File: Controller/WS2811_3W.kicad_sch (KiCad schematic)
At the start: 19 parts, among them J1 Conn_01x01_Female, J2 Conn_01x01_Female, J3 Conn_01x01_Female, J4 Conn_01x01_Female, J5 Conn_01x01_Female, J6 Conn_01x01_Female, U1 MAX485E, U2 WS2811, U3 MAX485E, U4 AMS1117-5.0

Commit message: pcb stuff
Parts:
- added J10, J11, J12, J7, J8, J9: Conn_01x01_Female, Connector_Wire:SolderWirePad_1x01_SMD_1x2mm, symbol Connector:Conn_01x01_Female
- added R6, R7, R8: 10k, Resistor_SMD:R_0603_1608Metric, symbol Device:R
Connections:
- net +5V: now also R6.1, R7.1, R8.1; no longer U1.8 (VCC)
- net DIM_B: now also R7.2
- net DIM_G: now also R8.2
- net DIM_R: now also R6.2
- net GND: no longer U1.2 (~RE), U1.3 (DE), U1.5 (GND)
- net WS_DIN: no longer U1.1 (RO)
- net at J2.1 (Pin_1), R1.2: no longer U1.6 (A)
- net at J1.1 (Pin_1), R1.1: no longer U1.7 (B)
- new net DCDC_CC/OUT+: J7.1 (Pin_1)
- new net DCDC_CC/OUT-: J8.1 (Pin_1)
- new net DCDC_CC1/OUT+: J9.1 (Pin_1)
- new net DCDC_CC1/OUT-: J10.1 (Pin_1)
- new net DCDC_CC2/OUT+: J11.1 (Pin_1)
- new net DCDC_CC2/OUT-: J12.1 (Pin_1)
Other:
- moved on the sheet: U1

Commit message: finish PCB
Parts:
- J5, J6: footprint Connector_Wire:SolderWirePad_1x01_SMD_1x2mm -> Techbeard:SolderWirePad_1x01_SMD_2x4mm
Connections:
- net +5V: now also U1.8 (VCC)
- net GND: now also U1.2 (~RE), U1.3 (DE), U1.5 (GND)
- net WS_DIN: now also U1.1 (RO)
- net at U1.6 (A): now also J2.1 (Pin_1), R1.2
- net at U1.7 (B): now also J1.1 (Pin_1), R1.1
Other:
- moved on the sheet: U1
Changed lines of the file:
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@@
     (property "Reference" "J5" (id 0) (at 170.3324 62.23 0))
     (property "Value" "Conn_01x01_Female" (id 1) (at 169.0624 67.31 0))
-    (property "Footprint" "Connector_Wire:SolderWirePad_1x01_SMD_1x2mm" (id 2) (at 168.91 64.77 0)
+    (property "Footprint" "Techbeard:SolderWirePad_1x01_SMD_2x4mm" (id 2) (at 168.91 64.77 0)
       (effects (font (size 1.27 1.27)) hide)
     )
@@
     (property "Reference" "J6" (id 0) (at 170.3324 69.85 0))
     (property "Value" "Conn_01x01_Female" (id 1) (at 165.2524 74.93 0))
-    (property "Footprint" "Connector_Wire:SolderWirePad_1x01_SMD_1x2mm" (id 2) (at 168.91 72.39 0)
+    (property "Footprint" "Techbeard:SolderWirePad_1x01_SMD_2x4mm" (id 2) (at 168.91 72.39 0)
       (effects (font (size 1.27 1.27)) hide)
     )
@@
     (pin "8")
   )
-  (symbol (lib_id "WS2811_3W-rescue:MAX485E-Interface_UART") (at 52.07 41.91 90) (mirror x) (unit 1)
-    (in_bom yes) (on_board yes)
-    (property "Reference" "U1" (id 0) (at 34.7726 41.91 0))
-    (property "Value" "MAX485E" (id 1) (at 37.084 41.91 0))
-    (property "Footprint" "Package_SO:SOIC-8_3.9x4.9mm_P1.27mm" (id 2) (at 69.85 41.91 0)
-      (effects (font (size 1.27 1.27)) hide)
-    )
-    (property "Datasheet" "https://datasheets.maximintegrated.com/en/ds/MAX1487E-MAX491E.pdf" (id 3) (at 50.8 41.91 0)
+  (symbol (lib_id "WS2811_3W-rescue:MAX485E-Interface_UART") (at 52.07 41.91 0) (mirror y) (unit 1)
+    (in_bom yes) (on_board yes)
+    (property "Reference" "U1" (id 0) (at 52.07 24.6126 0))
+    (property "Value" "MAX485E" (id 1) (at 52.07 26.924 0))
+    (property "Footprint" "Package_SO:SOIC-8_3.9x4.9mm_P1.27mm" (id 2) (at 52.07 59.69 0)
+      (effects (font (size 1.27 1.27)) hide)
+    )
+    (property "Datasheet" "https://datasheets.maximintegrated.com/en/ds/MAX1487E-MAX491E.pdf" (id 3) (at 52.07 40.64 0)
       (effects (font (size 1.27 1.27)) hide)
     )
@@
     (stroke (width 0.0006) (type solid) (color 0 0 0 0))
     (fill (color 0 0 0 0.0000))
-    (property "Schaltplanname" "DCDC_CC" (id 0) (at 134.62 88.2643 0)
+    (property "Sheet name" "DCDC_CC" (id 0) (at 134.62 88.2643 0)
       (effects (font (size 1.27 1.27)) (justify left bottom))
     )
-    (property "Dateiname Blatt" "DCDC_CC.kicad_sch" (id 1) (at 134.62 104.6487 0)
+    (property "Sheet file" "DCDC_CC.kicad_sch" (id 1) (at 134.62 104.6487 0)
       (effects (font (size 1.27 1.27)) (justify left top))
     )
@@
     (stroke (width 0.0006) (type solid) (color 0 0 0 0))
     (fill (color 0 0 0 0.0000))
-    (property "Schaltplanname" "DCDC_CC1" (id 0) (at 134.62 113.6643 0)
+    (property "Sheet name" "DCDC_CC1" (id 0) (at 134.62 113.6643 0)
       (effects (font (size 1.27 1.27)) (justify left bottom))
     )
-    (property "Dateiname Blatt" "DCDC_CC.kicad_sch" (id 1) (at 134.62 130.0487 0)
+    (property "Sheet file" "DCDC_CC.kicad_sch" (id 1) (at 134.62 130.0487 0)
       (effects (font (size 1.27 1.27)) (justify left top))
     )
@@
     (stroke (width 0.0006) (type solid) (color 0 0 0 0))
     (fill (color 0 0 0 0.0000))
-    (property "Schaltplanname" "DCDC_CC2" (id 0) (at 134.62 141.6043 0)
+    (property "Sheet name" "DCDC_CC2" (id 0) (at 134.62 141.6043 0)
       (effects (font (size 1.27 1.27)) (justify left bottom))
     )
-    (property "Dateiname Blatt" "DCDC_CC.kicad_sch" (id 1) (at 134.62 157.9887 0)
+    (property "Sheet file" "DCDC_CC.kicad_sch" (id 1) (at 134.62 157.9887 0)
       (effects (font (size 1.27 1.27)) (justify left top))
     )
@@
     )
     (path "/a5fcd8c9-66db-4541-bb43-1caff29d4253"
-      (reference "J5") (unit 1) (value "Conn_01x01_Female") (footprint "Connector_Wire:SolderWirePad_1x01_SMD_1x2mm")
+      (reference "J5") (unit 1) (value "Conn_01x01_Female") (footprint "Techbeard:SolderWirePad_1x01_SMD_2x4mm")
     )
     (path "/e723b894-1653-454d-9c2d-000f192c7ab3"
-      (reference "J6") (unit 1) (value "Conn_01x01_Female") (footprint "Connector_Wire:SolderWirePad_1x01_SMD_1x2mm")
+      (reference "J6") (unit 1) (value "Conn_01x01_Female") (footprint "Techbeard:SolderWirePad_1x01_SMD_2x4mm")
     )
     (path "/0dfc7477-9b4d-4490-aa8e-882655b7fb05"

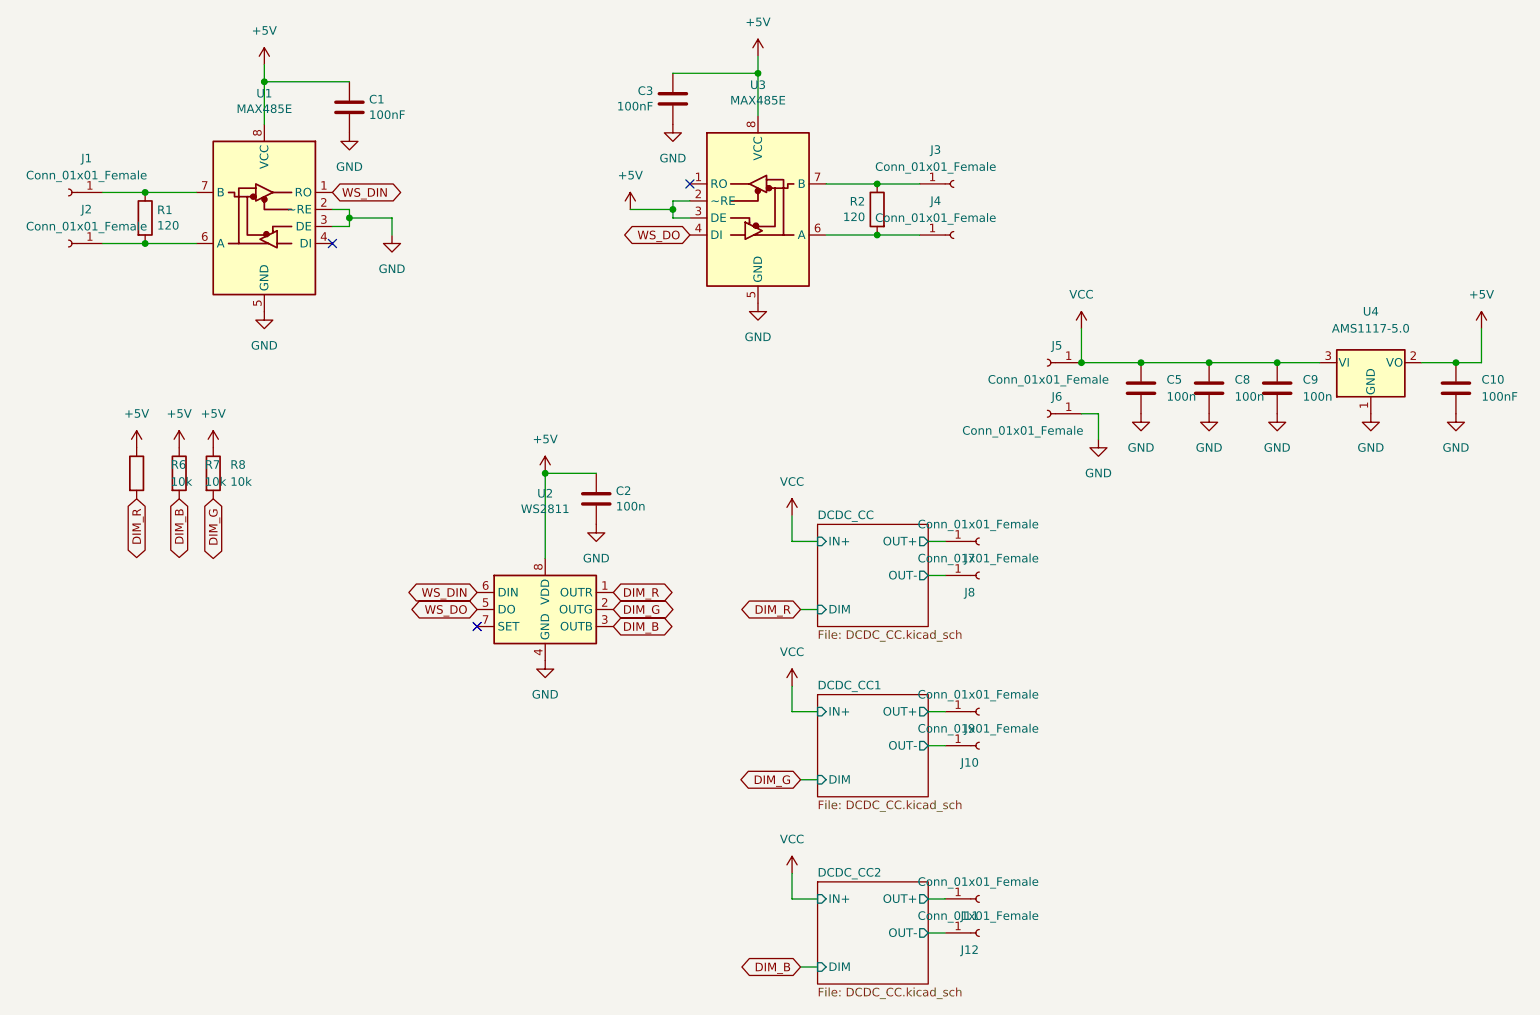
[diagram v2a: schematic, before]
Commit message: switch to different LDO
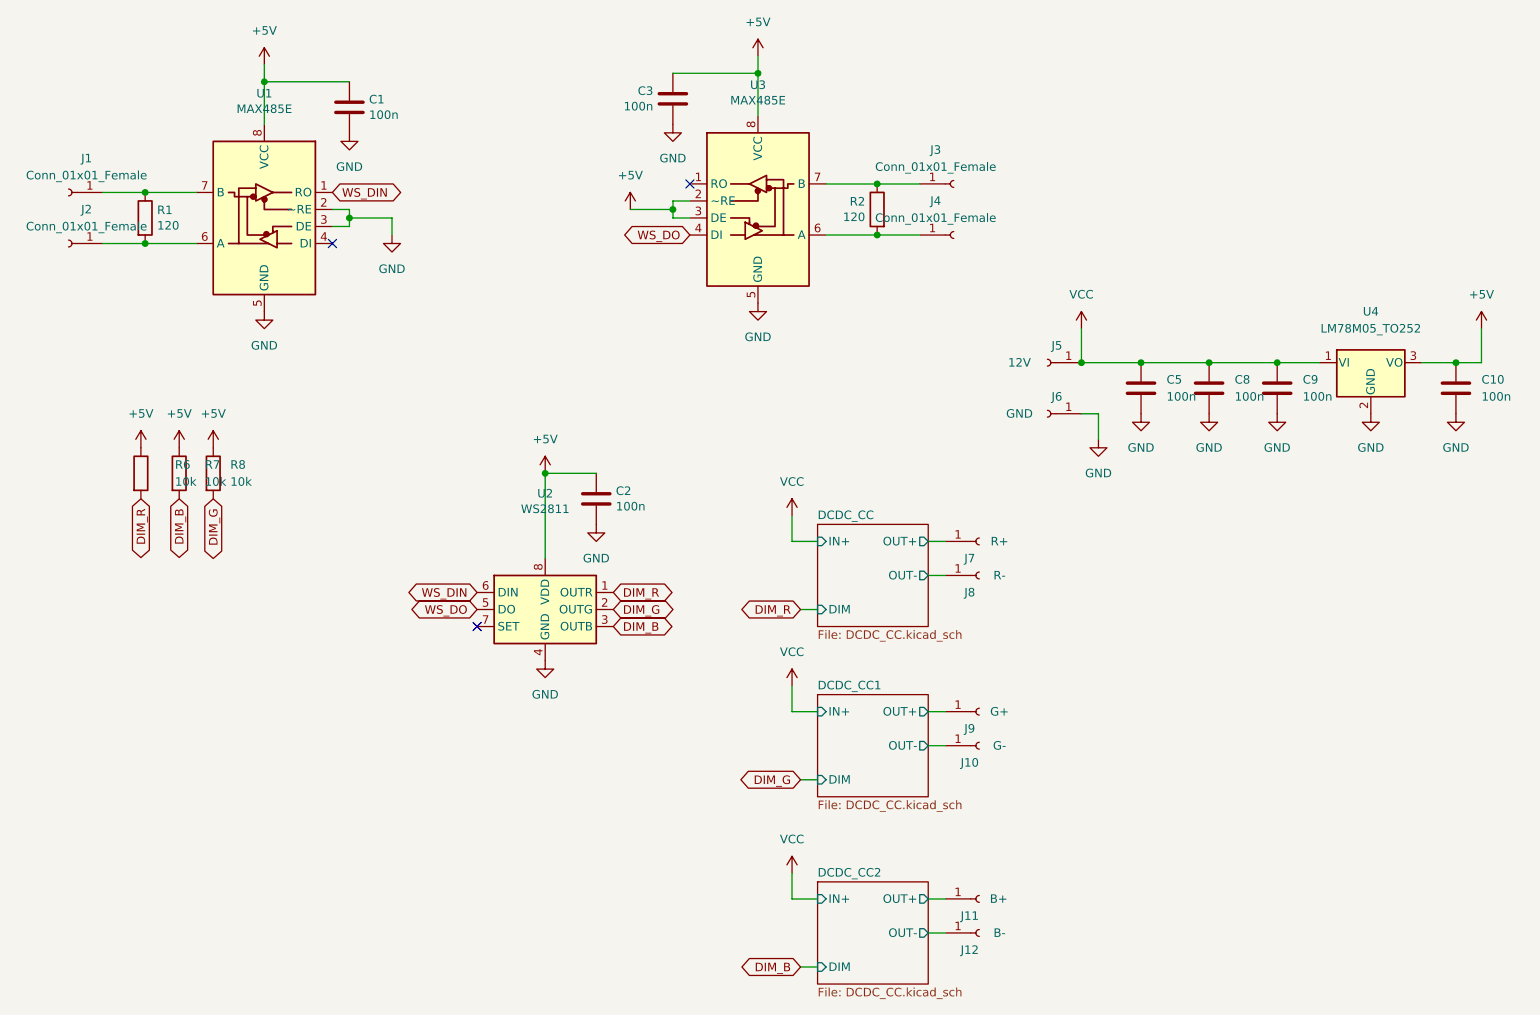
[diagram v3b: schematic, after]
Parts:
- removed U4: AMS1117-5.0, Package_TO_SOT_SMD:SOT-223-3_TabPin2, symbol Regulator_Linear:AMS1117-5.0
- added U4: LM78M05_TO252, Package_TO_SOT_SMD:TO-252-2, symbol Regulator_Linear:LM78M05_TO252
- C1, C10, C3: value 100nF -> 100n
- J10: value Conn_01x01_Female -> G-
- J11: value Conn_01x01_Female -> B+
- J12: value Conn_01x01_Female -> B-
- J5: value Conn_01x01_Female -> 12V
- J6: value Conn_01x01_Female -> GND
- J7: value Conn_01x01_Female -> R+
- J8: value Conn_01x01_Female -> R-
- J9: value Conn_01x01_Female -> G+
- R1, R2: now left out of the parts list
- U1, U3: LCSC (none) -> C444389
- U2: LCSC (none) -> C114581
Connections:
- net +5V: now also U4.3 (VO)
- net GND: now also U4.2 (GND)
- net VCC: now also U4.1 (VI)
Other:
- moved on the sheet: R6

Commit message: generate fabrication files
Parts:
- J1, J10, J11, J12, J2, J3, J4, J5, J6, J7, J8, J9: now left out of the parts list
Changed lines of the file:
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@@
   )
   (symbol (lib_id "Connector:Conn_01x01_Female") (at 22.86 39.37 180) (unit 1)
-    (in_bom yes) (on_board yes) (fields_autoplaced)
+    (in_bom no) (on_board yes) (fields_autoplaced)
     (property "Reference" "J1" (id 0) (at 25.5524 34.29 0))
     (property "Value" "Conn_01x01_Female" (id 1) (at 25.5524 36.83 0))
@@
   )
   (symbol (lib_id "Connector:Conn_01x01_Female") (at 22.86 46.99 180) (unit 1)
-    (in_bom yes) (on_board yes) (fields_autoplaced)
+    (in_bom no) (on_board yes) (fields_autoplaced)
     (property "Reference" "J2" (id 0) (at 25.5524 41.91 0))
     (property "Value" "Conn_01x01_Female" (id 1) (at 25.5524 44.45 0))
@@
   )
   (symbol (lib_id "Connector:Conn_01x01_Female") (at 154.94 38.1 0) (mirror x) (unit 1)
-    (in_bom yes) (on_board yes) (fields_autoplaced)
+    (in_bom no) (on_board yes) (fields_autoplaced)
     (property "Reference" "J3" (id 0) (at 152.2476 33.02 0))
     (property "Value" "Conn_01x01_Female" (id 1) (at 152.2476 35.56 0))
@@
   )
   (symbol (lib_id "Connector:Conn_01x01_Female") (at 154.94 45.72 0) (mirror x) (unit 1)
-    (in_bom yes) (on_board yes) (fields_autoplaced)
+    (in_bom no) (on_board yes) (fields_autoplaced)
     (property "Reference" "J4" (id 0) (at 152.2476 40.64 0))
     (property "Value" "Conn_01x01_Female" (id 1) (at 152.2476 43.18 0))
@@
   )
   (symbol (lib_id "Connector:Conn_01x01_Female") (at 158.75 91.44 0) (mirror x) (unit 1)
-    (in_bom yes) (on_board yes)
+    (in_bom no) (on_board yes)
     (property "Reference" "J7" (id 0) (at 157.3276 93.98 0))
     (property "Value" "R+" (id 1) (at 161.7726 91.44 0))
@@
   )
   (symbol (lib_id "Connector:Conn_01x01_Female") (at 158.75 96.52 0) (mirror x) (unit 1)
-    (in_bom yes) (on_board yes)
+    (in_bom no) (on_board yes)
     (property "Reference" "J8" (id 0) (at 157.3276 99.06 0))
     (property "Value" "R-" (id 1) (at 161.7726 96.52 0))
@@
   )
   (symbol (lib_id "Connector:Conn_01x01_Female") (at 158.75 116.84 0) (mirror x) (unit 1)
-    (in_bom yes) (on_board yes)
+    (in_bom no) (on_board yes)
     (property "Reference" "J9" (id 0) (at 157.3276 119.38 0))
     (property "Value" "G+" (id 1) (at 161.7726 116.84 0))
@@
   )
   (symbol (lib_id "Connector:Conn_01x01_Female") (at 158.75 121.92 0) (mirror x) (unit 1)
-    (in_bom yes) (on_board yes)
+    (in_bom no) (on_board yes)
     (property "Reference" "J10" (id 0) (at 157.3276 124.46 0))
     (property "Value" "G-" (id 1) (at 161.7726 121.92 0))
@@
   )
   (symbol (lib_id "Connector:Conn_01x01_Female") (at 158.75 144.78 0) (mirror x) (unit 1)
-    (in_bom yes) (on_board yes)
+    (in_bom no) (on_board yes)
     (property "Reference" "J11" (id 0) (at 157.3276 147.32 0))
     (property "Value" "B+" (id 1) (at 161.6456 144.78 0))
@@
   )
   (symbol (lib_id "Connector:Conn_01x01_Female") (at 158.75 149.86 0) (mirror x) (unit 1)
-    (in_bom yes) (on_board yes)
+    (in_bom no) (on_board yes)
     (property "Reference" "J12" (id 0) (at 157.3276 152.4 0))
     (property "Value" "B-" (id 1) (at 161.7726 149.86 0))
@@
   )
   (symbol (lib_id "Connector:Conn_01x01_Female") (at 168.91 64.77 0) (mirror y) (unit 1)
-    (in_bom yes) (on_board yes)
+    (in_bom no) (on_board yes)
     (property "Reference" "J5" (id 0) (at 170.3324 62.23 0))
     (property "Value" "12V" (id 1) (at 164.7444 64.77 0))
@@
   )
   (symbol (lib_id "Connector:Conn_01x01_Female") (at 168.91 72.39 0) (mirror y) (unit 1)
-    (in_bom yes) (on_board yes)
+    (in_bom no) (on_board yes)
     (property "Reference" "J6" (id 0) (at 170.3324 69.85 0))
     (property "Value" "GND" (id 1) (at 164.7444 72.39 0))
@@
     )
     (path "/5be75f30-d276-492a-9eb9-21a40b23ff24/e8f3dd54-0238-4ce5-a992-69056eca88dc"
-      (reference "D4") (unit 1) (value "40V 1A") (footprint "Diode_SMD:D_SOD-123")
+      (reference "D4") (unit 1) (value "40V 1A Schottky") (footprint "Diode_SMD:D_SOD-123")
     )
     (path "/1b355707-52f8-4151-ad6c-4e12a31e649f/e8f3dd54-0238-4ce5-a992-69056eca88dc"
-      (reference "D5") (unit 1) (value "40V 1A") (footprint "Diode_SMD:D_SOD-123")
+      (reference "D5") (unit 1) (value "40V 1A Schottky") (footprint "Diode_SMD:D_SOD-123")
     )
     (path "/fb3b30b3-b2bc-41fe-aeeb-c16cf599aed4/e8f3dd54-0238-4ce5-a992-69056eca88dc"
-      (reference "D6") (unit 1) (value "40V 1A") (footprint "Diode_SMD:D_SOD-123")
+      (reference "D6") (unit 1) (value "40V 1A Schottky") (footprint "Diode_SMD:D_SOD-123")
     )
     (path "/6bbb4c7d-56ba-4a53-993d-82aa5d97a0e3"
